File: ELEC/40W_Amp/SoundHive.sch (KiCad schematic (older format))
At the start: 3 parts, among them J1 CONN_01X08, J2 CONN_01X08, U1 TPA3106D1

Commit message: Paths updated and stuff
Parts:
- J2: footprint (none) -> Pin_Headers:Pin_Header_Angled_1x08
- U1: footprint ~ -> (none)
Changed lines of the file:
@@
 EESchema Schematic File Version 2
 LIBS:conn
-LIBS:ClassD_Audio
-EELAYER 27 0
+LIBS:SoundHive-cache
+EELAYER 25 0
 EELAYER END
 $Descr A4 11693 8268
@@
 F 0 "U1" H 4250 3800 60  0000 C CNN
 F 1 "TPA3106D1" H 4450 3900 60  0000 C CNN
-F 2 "~" H 4850 3100 60  0000 C CNN
+F 2 "" H 4850 3100 60  0000 C CNN
 F 3 "~" H 4850 3100 60  0000 C CNN
 	1    5150 3050
@@
 F 0 "J2" H 9100 3500 50  0000 C CNN
 F 1 "CONN_01X08" V 9200 3050 50  0000 C CNN
-F 2 "" H 9100 3050 50  0001 C CNN
+F 2 "Pin_Headers:Pin_Header_Angled_1x08" H 9100 3050 50  0001 C CNN
 F 3 "" H 9100 3050 50  0001 C CNN
 	1    9100 3050

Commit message: -Still rolling
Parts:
- added L1, L2: XAL6060-333ME 33uH, Inductors:XAL6060-333ME, symbol L
- J1: footprint (none) -> Pin_Headers:Pin_Header_Straight_1x08_Pitch2.54mm
- J2: footprint Pin_Headers:Pin_Header_Angled_1x08 -> Pin_Headers:Pin_Header_Straight_1x08_Pitch2.54mm
- U1: footprint (none) -> Houseings_QFP_Walker:LQFP-32_7x7mm_Pitch0.8mm-EP
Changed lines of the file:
@@
 EESchema Schematic File Version 2
 LIBS:conn
+LIBS:ClassD_Audio
+LIBS:device
 LIBS:SoundHive-cache
 EELAYER 25 0
@@
 U 1 1 5927C849
 P 5150 3050
-F 0 "U1" H 4250 3800 60  0000 C CNN
-F 1 "TPA3106D1" H 4450 3900 60  0000 C CNN
-F 2 "" H 4850 3100 60  0000 C CNN
-F 3 "~" H 4850 3100 60  0000 C CNN
+F 0 "U1" H 4100 3700 60  0000 C CNN
+F 1 "TPA3106D1" H 4300 3800 60  0000 C CNN
+F 2 "Houseings_QFP_Walker:LQFP-32_7x7mm_Pitch0.8mm-EP" H 4800 3050 60  0001 C CNN
+F 3 "~" H 4800 3050 60  0000 C CNN
 	1    5150 3050
 	1    0    0    -1
@@
 F 0 "J2" H 9100 3500 50  0000 C CNN
 F 1 "CONN_01X08" V 9200 3050 50  0000 C CNN
-F 2 "Pin_Headers:Pin_Header_Angled_1x08" H 9100 3050 50  0001 C CNN
+F 2 "Pin_Headers:Pin_Header_Straight_1x08_Pitch2.54mm" H 9100 3050 50  0001 C CNN
 F 3 "" H 9100 3050 50  0001 C CNN
 	1    9100 3050
@@
 F 0 "J1" H 8150 3500 50  0000 C CNN
 F 1 "CONN_01X08" V 8250 3050 50  0000 C CNN
-F 2 "" H 8150 3050 50  0001 C CNN
+F 2 "Pin_Headers:Pin_Header_Straight_1x08_Pitch2.54mm" H 8150 3050 50  0001 C CNN
 F 3 "" H 8150 3050 50  0001 C CNN
 	1    8150 3050
 	-1   0    0    1
 $EndComp
+$Comp
+L L L1
+U 1 1 59362A9C
+P 6900 3200
+F 0 "L1" V 6850 3200 50  0000 C CNN
+F 1 "XAL6060-333ME 33uH" V 6975 3200 50  0000 C CNN
+F 2 "Inductors:XAL6060-333ME" H 6900 3200 50  0001 C CNN
+F 3 "" H 6900 3200 50  0001 C CNN
+	1    6900 3200
+	0    -1   -1   0
+$EndComp
+$Comp
+L L L2
+U 1 1 59362C26
+P 6900 2900
+F 0 "L2" V 6850 2900 50  0000 C CNN
+F 1 "XAL6060-333ME 33uH" V 6975 2900 50  0000 C CNN
+F 2 "Inductors:XAL6060-333ME" H 6900 2900 50  0001 C CNN
+F 3 "" H 6900 2900 50  0001 C CNN
+	1    6900 2900
+	0    -1   -1   0
+$EndComp
 $EndSCHEMATC

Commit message: Parts and stuff
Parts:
- added C1, C2: 1.0uF, Capacitors_SMD:C_0805, symbol C
- L1: value XAL6060-333ME 33uH -> 33uH; Part Number (none) -> XAL6060-333ME
- L2: value XAL6060-333ME 33uH -> 33uH; Part Number (none) -> 33uH
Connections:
- net at U1.1 (INP): now also C1.1
- net at U1.19 (OUTN): now also L1.1, U1.20 (OUTN)
- net at U1.2 (INN): now also C2.1
- net at U1.21 (OUTP): now also L2.1, U1.22 (OUTP)
- net GND: now reaches U1.3 (AGND)
- net GND: now also U1.4 (AGND)
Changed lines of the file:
@@
 LIBS:ClassD_Audio
 LIBS:device
+LIBS:power
 LIBS:SoundHive-cache
 EELAYER 25 0
@@
 P 6900 3200
 F 0 "L1" V 6850 3200 50  0000 C CNN
-F 1 "XAL6060-333ME 33uH" V 6975 3200 50  0000 C CNN
+F 1 "33uH" V 6975 3200 50  0000 C CNN
 F 2 "Inductors:XAL6060-333ME" H 6900 3200 50  0001 C CNN
 F 3 "" H 6900 3200 50  0001 C CNN
+F 4 "XAL6060-333ME" V 6900 3200 60  0001 C CNN "Part Number"
 	1    6900 3200
 	0    -1   -1   0
@@
 P 6900 2900
 F 0 "L2" V 6850 2900 50  0000 C CNN
-F 1 "XAL6060-333ME 33uH" V 6975 2900 50  0000 C CNN
+F 1 "33uH" V 6975 2900 50  0000 C CNN
 F 2 "Inductors:XAL6060-333ME" H 6900 2900 50  0001 C CNN
 F 3 "" H 6900 2900 50  0001 C CNN
+F 4 "33uH" V 6900 2900 60  0001 C CNN "Part Number"
 	1    6900 2900
 	0    -1   -1   0
 $EndComp
+$Comp
+L C C1
+U 1 1 59364072
+P 3450 2650
+F 0 "C1" H 3475 2750 50  0000 L CNN
+F 1 "1.0uF" V 3300 2550 50  0000 L CNN
+F 2 "Capacitors_SMD:C_0805" H 3488 2500 50  0001 C CNN
+F 3 "" H 3450 2650 50  0001 C CNN
+	1    3450 2650
+	0    1    1    0
+$EndComp
+$Comp
+L C C2
+U 1 1 593640E9
+P 3450 2950
+F 0 "C2" H 3475 3050 50  0000 L CNN
+F 1 "1.0uF" V 3300 2850 50  0000 L CNN
+F 2 "Capacitors_SMD:C_0805" H 3488 2800 50  0001 C CNN
+F 3 "" H 3450 2950 50  0001 C CNN
+	1    3450 2950
+	0    1    1    0
+$EndComp
+Wire Wire Line
+	4200 2800 3750 2800
+$Comp
+L GND #PWR01
+U 1 1 593640FB
+P 6600 4800
+F 0 "#PWR01" H 6600 4550 50  0001 C CNN
+F 1 "GND" H 6600 4650 50  0000 C CNN
+F 2 "" H 6600 4800 50  0001 C CNN
+F 3 "" H 6600 4800 50  0001 C CNN
+	1    6600 4800
+	1    0    0    -1
+$EndComp
+$Comp
+L GNDA #PWR02
+U 1 1 5936417F
+P 6850 4800
+F 0 "#PWR02" H 6850 4550 50  0001 C CNN
+F 1 "GNDA" H 6850 4650 50  0000 C CNN
+F 2 "" H 6850 4800 50  0001 C CNN
+F 3 "" H 6850 4800 50  0001 C CNN
+	1    6850 4800
+	1    0    0    -1
+$EndComp
+Wire Wire Line
+	6600 4800 6850 4800
+Wire Wire Line
+	4200 3000 4100 3000
+Wire Wire Line
+	4100 3000 4100 2900
+Wire Wire Line
+	4100 2900 4200 2900
+$Comp
+L GNDA #PWR03
+U 1 1 593642E8
+P 3850 3000
+F 0 "#PWR03" H 3850 2750 50  0001 C CNN
+F 1 "GNDA" H 3850 2850 50  0000 C CNN
+F 2 "" H 3850 3000 50  0001 C CNN
+F 3 "" H 3850 3000 50  0001 C CNN
+	1    3850 3000
+	1    0    0    -1
+$EndComp
+Wire Wire Line
+	4100 2950 3850 2950
+Wire Wire Line
+	3850 2950 3850 3000
+Connection ~ 4100 2950
+Wire Wire Line
+	6150 2900 6750 2900
+Wire Wire Line
+	6150 3000 6300 3000
+Wire Wire Line
+	6300 3000 6300 2900
+Connection ~ 6300 2900
+Wire Wire Line
+	6150 3100 6300 3100
+Wire Wire Line
+	6300 3100 6300 3200
+Wire Wire Line
+	6150 3200 6750 3200
+Connection ~ 6300 3200
+Wire Wire Line
+	3750 2800 3750 2950
+Wire Wire Line
+	3750 2950 3600 2950
+Wire Wire Line
+	4200 2700 3750 2700
+Wire Wire Line
+	3750 2700 3750 2650
+Wire Wire Line
+	3750 2650 3600 2650
 $EndSCHEMATC

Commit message: Layout changes, Tall headers added
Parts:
- J1, J2: footprint Pin_Headers:Pin_Header_Straight_1x08_Pitch2.54mm -> Pin_Headers:Pin_Header_Straight_1x08_Tall_Pitch2.54mm
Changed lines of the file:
@@
 F 0 "J2" H 9100 3500 50  0000 C CNN
 F 1 "CONN_01X08" V 9200 3050 50  0000 C CNN
-F 2 "Pin_Headers:Pin_Header_Straight_1x08_Pitch2.54mm" H 9100 3050 50  0001 C CNN
+F 2 "Pin_Headers:Pin_Header_Straight_1x08_Tall_Pitch2.54mm" H 9100 3050 50  0001 C CNN
 F 3 "" H 9100 3050 50  0001 C CNN
 	1    9100 3050
@@
 F 0 "J1" H 8150 3500 50  0000 C CNN
 F 1 "CONN_01X08" V 8250 3050 50  0000 C CNN
-F 2 "Pin_Headers:Pin_Header_Straight_1x08_Pitch2.54mm" H 8150 3050 50  0001 C CNN
+F 2 "Pin_Headers:Pin_Header_Straight_1x08_Tall_Pitch2.54mm" H 8150 3050 50  0001 C CNN
 F 3 "" H 8150 3050 50  0001 C CNN
 	1    8150 3050

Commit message: Major work.
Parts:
- added C10, C11: 0.22uF, Capacitors_SMD:C_0805, symbol C
- added C12, C13: 1nF COG, Capacitors_SMD:C_0805, symbol C
- added C14, C15, C4, C6, C7, C8, C9: 1.0uF, Capacitors_SMD:C_0805, symbol C
- added C3, C5: 220uF, Capacitors_SMD:CP_Elec_8x10.5, symbol CP1
- added R1, R2: 100K, Resistors_SMD:R_0805, symbol R
- added R3: 100K 1%, Resistors_SMD:R_0805, symbol R
- added R4, R?: 20R 1/4 W, 5%, Resistors_SMD:R_1206, symbol R
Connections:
- net GND: now also U1.12 (AGND), U1.16 (PGND), U1.17 (PGND), U1.24 (PGND), U1.25 (PGND), C14.1, C15.2, C3.2, C4.1, C5.2, C6.1, C7.1, C8.1, C9.1, R3.2, R4.1, R?.2
- net at U1.10 (VREG): now also C7.2, R1.2, R2.2
- net at U1.11 (VBYP): now also C8.2
- net at U1.13 (VCLAMP): now also C9.2
- net +24V: now reaches U1.14 (PVCC)
- net +24V: now also U1.15 (PVCC), U1.26 (PVCC), U1.27 (PVCC), U1.28 (PVCC), C3.1, C4.2, C5.1, C6.2
- net at U1.18 (BSN): now also C11.1
- net at L1.1, U1.19 (OUTN), U1.20 (OUTN): now also C11.2, C13.2
- net at L2.1, U1.21 (OUTP), U1.22 (OUTP): now also C10.1, C12.1
- net at U1.23 (BSP): now also C10.2
- net GAIN0: now reaches U1.5 (GAIN0)
- net GAIN0: now also R1.1
- net GAIN1: now reaches U1.6 (GAIN1)
- net GAIN1: now also R2.1
- net at U1.9 (ROSC): now also R3.1
- net at L1.2: now also C15.1
- net at L2.2: now also C14.2
- new net: C12.2, R4.2
- new net: C13.1, R?.1
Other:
- note added: "MSTR/SLV need to go to a jumper\nthen the sync pins needs to be tied\nthrough the headers. The headers \nneed to be close to the chip!."
- note added: "Most likely the speaker configuration can \nbe set w/ these gain jumpers (8ohm or 4ohm)"
- moved on the sheet: C1, C2, J1, J2, L1, L2, U1

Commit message: Changed paths (Used  ${KIPRJMOD})
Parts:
- gave numbers to parts that had none: 1
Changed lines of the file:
@@
 MSTR/SLV need to go to a jumper\nthen the sync pins needs to be tied\nthrough the headers. The headers \nneed to be close to the chip!.
 $Comp
-L R R?
+L R R5
 U 1 1 59383A68
 P 7400 4700
-F 0 "R?" V 7600 4700 50  0000 C CNN
+F 0 "R5" V 7600 4700 50  0000 C CNN
 F 1 "20R 1/4 W, 5%" V 7500 4700 50  0000 C CNN
 F 2 "Resistors_SMD:R_1206" V 7330 4700 50  0001 C CNN

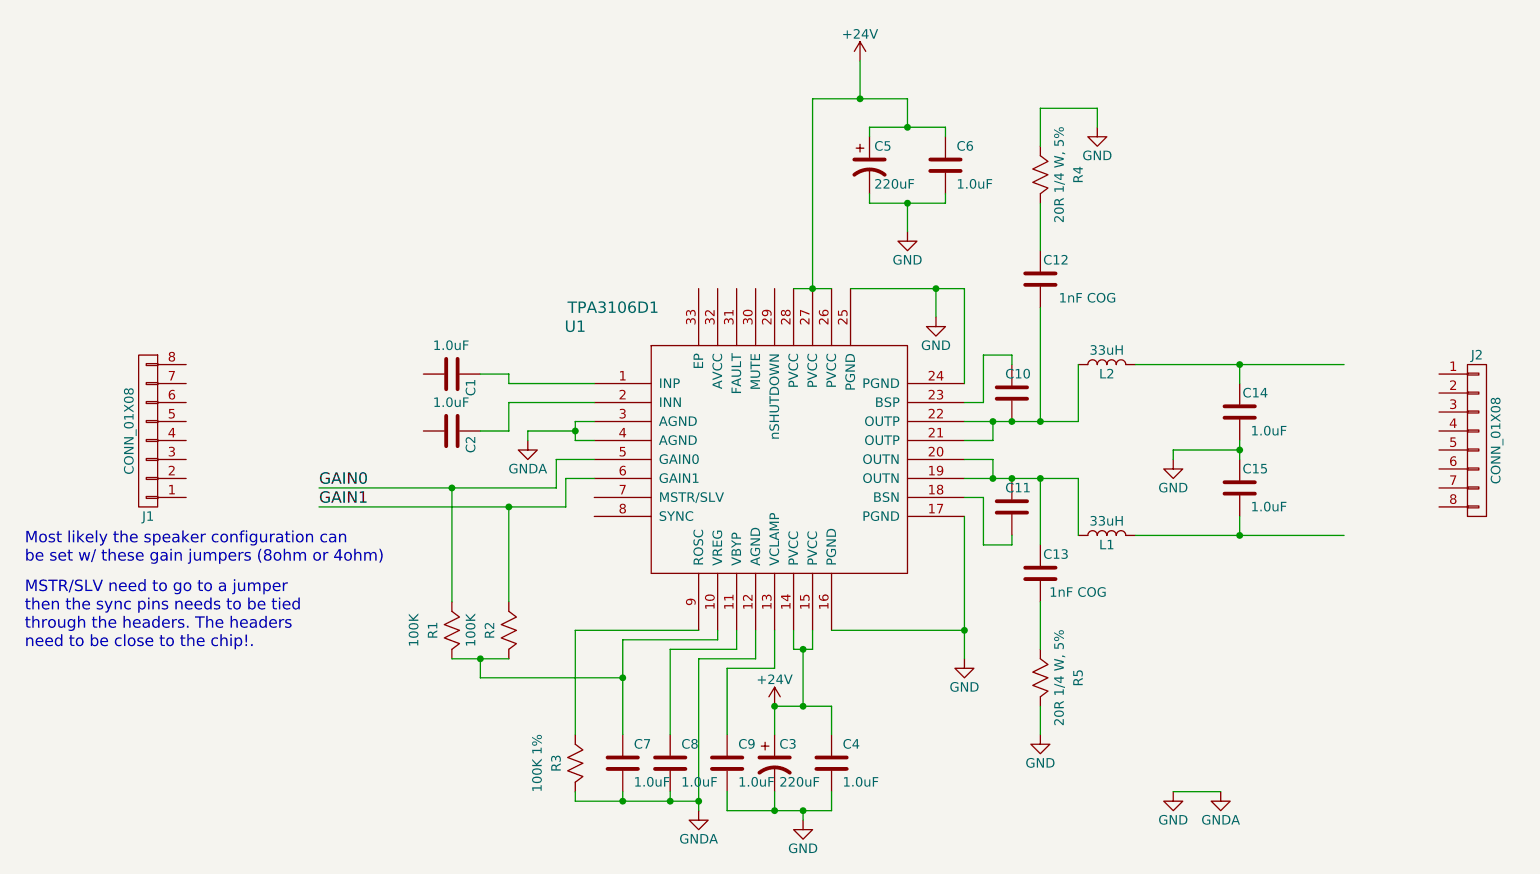
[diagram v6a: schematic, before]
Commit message: Added connector, redecorated.
Consider changing 2.54mm pich headers to somethin smaller
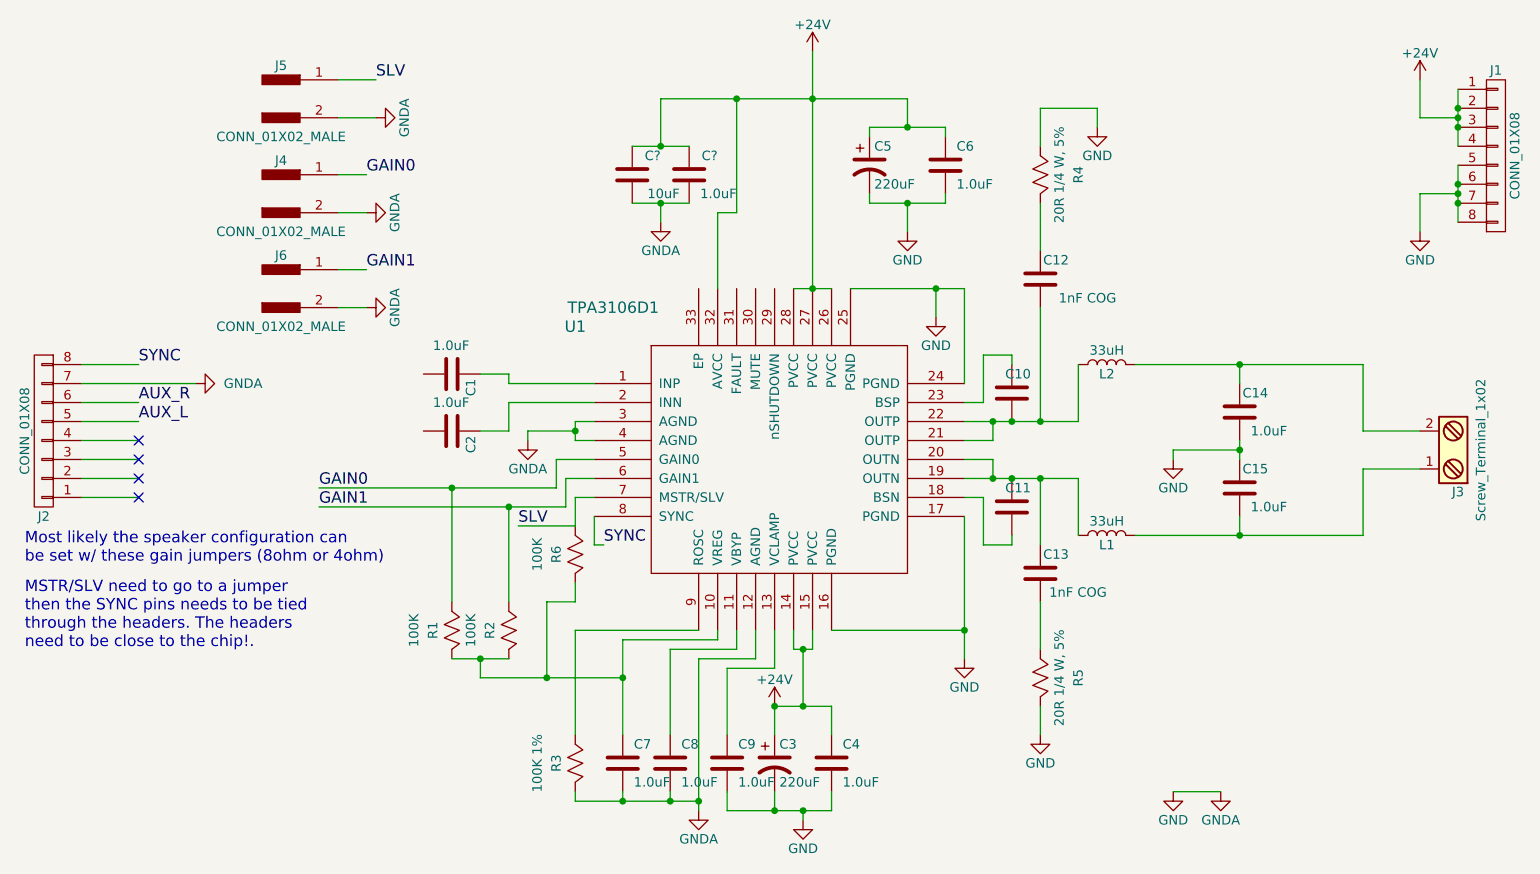
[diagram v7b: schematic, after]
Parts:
- added C?: 1.0uF, Capacitors_SMD:C_0805, symbol C
- added C?: 10uF, Capacitors_SMD:C_0805, symbol C
- added J3: Screw_Terminal_1x02, Connectors_Terminal_Blocks.pretty:TerminalBlock_Pheonix_MKDS1.5-2pol, symbol Screw_Terminal_1x02
- added J4, J5, J6: CONN_01X02_MALE, Pin_Headers:Pin_Header_Angled_1x02_Pitch2.54mm, symbol CONN_01X02_MALE
- added R6: 100K, Resistors_SMD:R_0805, symbol R
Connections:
- net +24V: now also J1.1 (P1), J1.2 (P2), J1.3 (P3), J1.4 (P4), U1.32 (AVCC), C?.2, C?.2
- net GAIN0: now also J4.1
- net GAIN1: now also J6.1
- net GND: now also J1.5 (P5), J1.6 (P6), J1.7 (P7), J1.8 (P8), J2.7 (P7), C?.1, C?.1, J4.2, J5.2, J6.2
- net at C7.2, R1.2, R2.2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: now also R6.2
- net SLV: now reaches U1.7 (MSTR/SLV)
- net SLV: now also J5.1, R6.1
- net SYNC: now reaches U1.8 (SYNC)
- net SYNC: now also J2.8 (P8)
- net AUX_L: now reaches J2.5 (P5)
- net AUX_R: now reaches J2.6 (P6)
- net at C15.1, L1.2: now also J3.1
- net at C14.2, L2.2: now also J3.2
- no-connect marks 0 -> 4
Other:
- note added: "MSTR/SLV need to go to a jumper\nthen the SYNC pins needs to be tied\nthrough the headers. The headers \nneed to be close to the chip!."
- note removed: "MSTR/SLV need to go to a jumper\nthen the sync pins needs to be tied\nthrough the headers. The headers \nneed to be close to the chip!."
- moved on the sheet: J1, J2

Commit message: -Moved all 3D models into project -This should be how we move forward. System paths are too flakey
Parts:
- added J7: CONN_01X03_MALE, Pin_Headers:Pin_Header_Angled_1x03_Pitch2.54mm, symbol CONN_01X03_MALE
- gave numbers to parts that had none: 2
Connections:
- net AUX_L: now also J7.3
- net AUX_R: now also J7.1
- net GND: now also C2.2
- net LR_MuxOut: now reaches C1.2
- net LR_MuxOut: now also J7.2
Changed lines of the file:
@@
 $EndComp
 $Comp
-L +24V #PWR?
+L +24V #PWR018
 U 1 1 593E5732
 P 9400 1550
-F 0 "#PWR?" H 9400 1400 50  0001 C CNN
+F 0 "#PWR018" H 9400 1400 50  0001 C CNN
 F 1 "+24V" H 9400 1690 50  0000 C CNN
 F 2 "" H 9400 1550 50  0001 C CNN
@@
 Connection ~ 9600 2200
 $Comp
-L GND #PWR?
+L GND #PWR019
 U 1 1 593E5FB4
 P 9400 2350
-F 0 "#PWR?" H 9400 2100 50  0001 C CNN
+F 0 "#PWR019" H 9400 2100 50  0001 C CNN
 F 1 "GND" H 9400 2200 50  0000 C CNN
 F 2 "" H 9400 2350 50  0001 C CNN
@@
 NoConn ~ 2650 3750
 $Comp
-L C C?
+L C C17
 U 1 1 593E7796
 P 5550 2050
-F 0 "C?" H 5400 1950 50  0000 L CNN
+F 0 "C17" H 5400 1950 50  0000 L CNN
 F 1 "1.0uF" H 5300 2150 50  0000 L CNN
 F 2 "Capacitors_SMD:C_0805" H 5588 1900 50  0001 C CNN
@@
 $EndComp
 $Comp
-L C C?
+L C C16
 U 1 1 593E7861
 P 5250 2050
-F 0 "C?" H 5100 1950 50  0000 L CNN
+F 0 "C16" H 5100 1950 50  0000 L CNN
 F 1 "10uF" H 5000 2150 50  0000 L CNN
 F 2 "Capacitors_SMD:C_0805" H 5288 1900 50  0001 C CNN
@@
 Connection ~ 5800 1650
 $Comp
-L GNDA #PWR?
+L GNDA #PWR020
 U 1 1 593E89C7
 P 5400 2300
-F 0 "#PWR?" H 5400 2050 50  0001 C CNN
+F 0 "#PWR020" H 5400 2050 50  0001 C CNN
 F 1 "GNDA" H 5400 2150 50  0000 C CNN
 F 2 "" H 5400 2300 50  0001 C CNN
@@
 	1    0    0    -1
 $EndComp
+$Comp
+L GNDA #PWR021
+U 1 1 593F51C4
+P 3950 3400
+F 0 "#PWR021" H 3950 3150 50  0001 C CNN
+F 1 "GNDA" H 3950 3250 50  0000 C CNN
+F 2 "" H 3950 3400 50  0001 C CNN
+F 3 "" H 3950 3400 50  0001 C CNN
+	1    3950 3400
+	0    1    1    0
+$EndComp
+Wire Wire Line
+	4150 3400 3950 3400
+$Comp
+L CONN_01X03_MALE J7
+U 1 1 593F55A4
+P 3100 5100
+F 0 "J7" H 3100 5375 50  0000 C CNN
+F 1 "CONN_01X03_MALE" H 3125 4825 50  0000 C CNN
+F 2 "Pin_Headers:Pin_Header_Angled_1x03_Pitch2.54mm" H 3100 5300 50  0001 C CNN
+F 3 "" H 3100 5300 50  0001 C CNN
+	1    3100 5100
+	1    0    0    -1
+$EndComp
+Wire Wire Line
+	3400 5100 3750 5100
+Text Label 3750 5100 0    60   ~ 0
+LR_MuxOut
+Wire Wire Line
+	3400 4900 3750 4900
+Wire Wire Line
+	3400 5300 3750 5300
+Text Label 3750 4900 0    60   ~ 0
+AUX_R
+Text Label 3750 5300 0    60   ~ 0
+AUX_L
+Text Label 3600 3100 0    60   ~ 0
+LR_MuxOut
+Wire Wire Line
+	4150 3100 3600 3100
 $EndSCHEMATC
